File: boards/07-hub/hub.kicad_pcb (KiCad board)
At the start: 2 copper layers, 130 x 98 mm, 28 parts, among them J1 USB_B, J2 BUS, J3 BUS, J4 BUS, J5 BUS, J6 BUS, J7 BUS, J8 BUS, J9 BUS

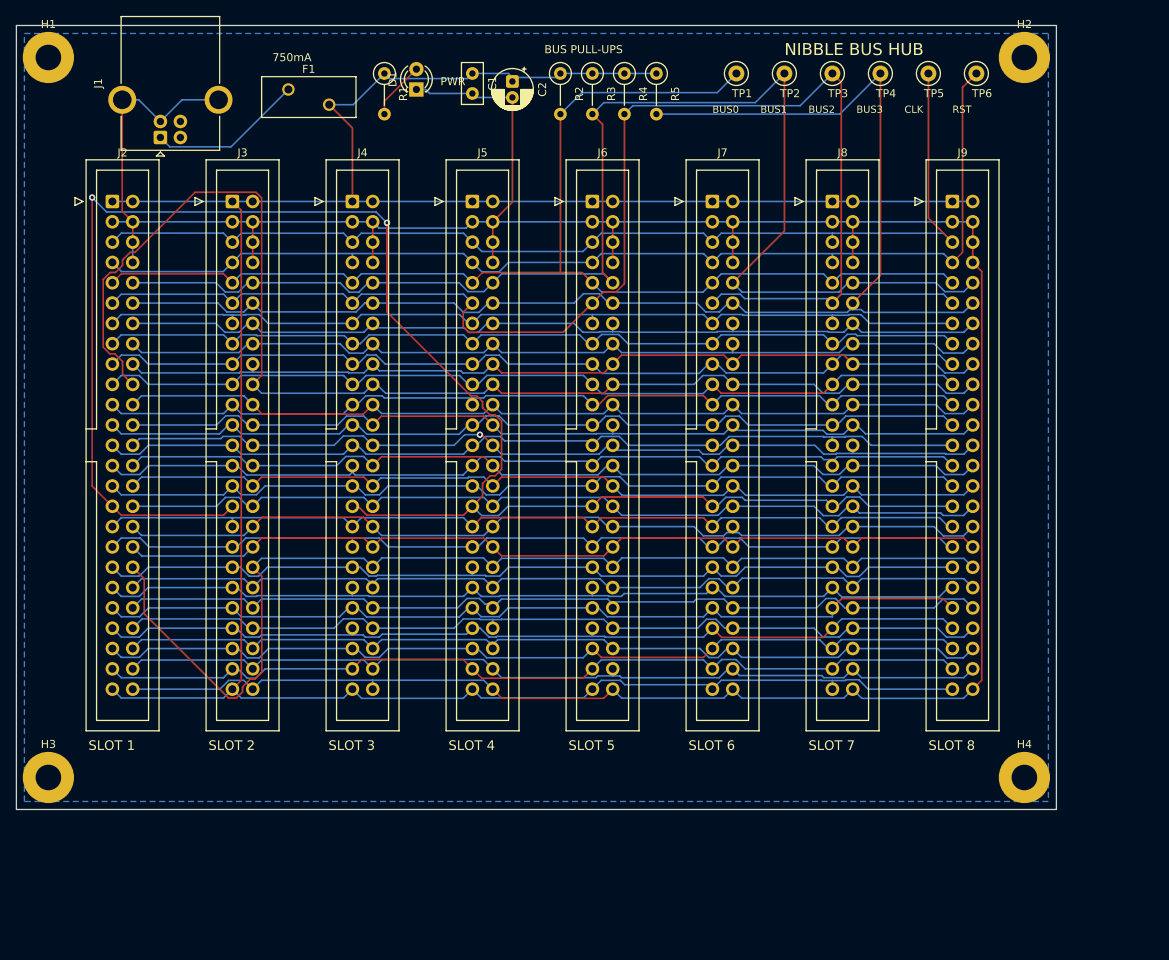
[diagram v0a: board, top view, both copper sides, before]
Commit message: Hub routed: DRC zero, nothing unconnected
The test loops sat on the corner mounting hole and on the last header's
courtyard; they are a 3 x 2 block between the bus pull-ups and the hole now.

Co-Authored-By: Claude Fable 5.1 <noreply@anthropic.com>
Claude-Session: https://claude.ai/code/session_019vcbW37ERmrjZaWq55Er3J
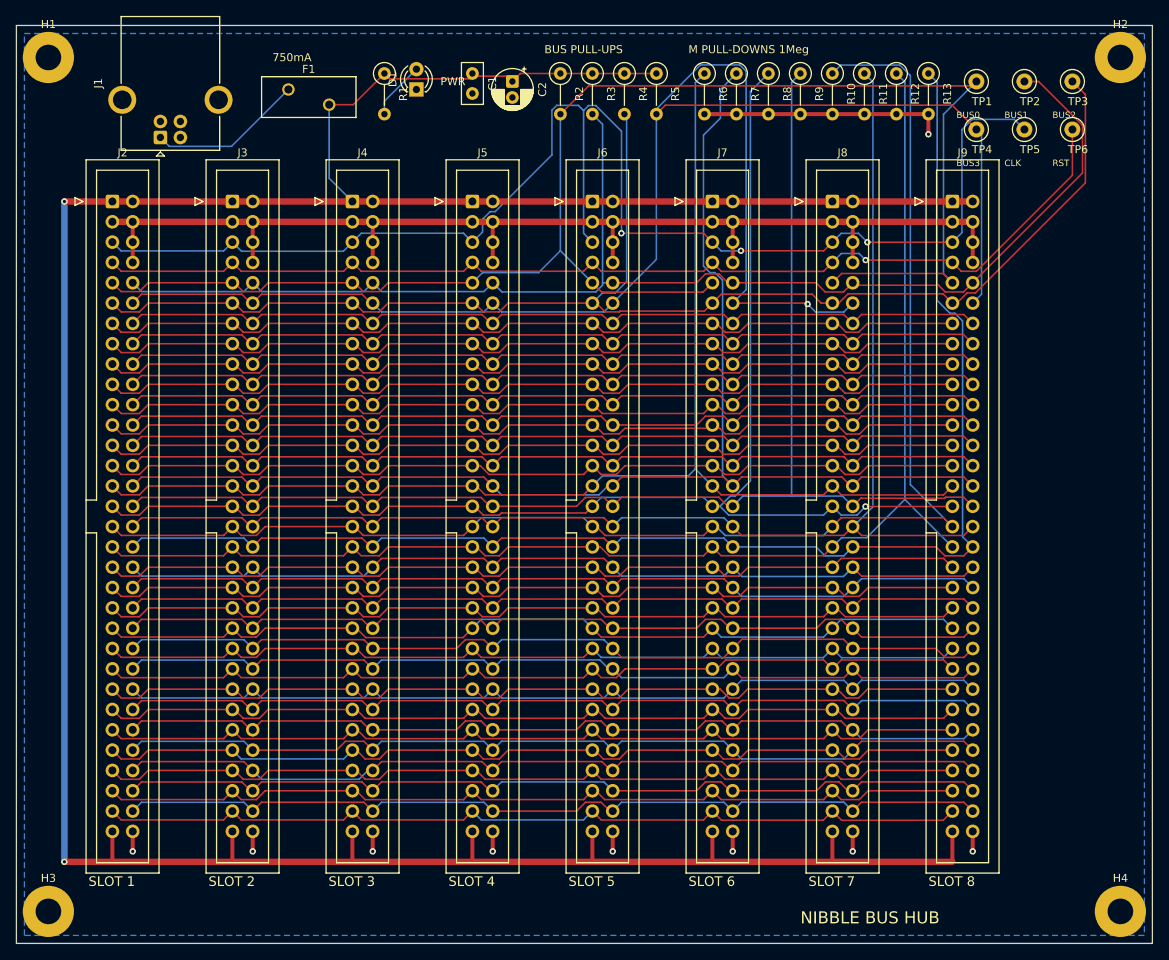
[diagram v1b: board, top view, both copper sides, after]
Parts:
- added R10: 1Meg, R_Axial_DIN0207_L6.3mm_D2.5mm_P5.08mm_Vertical, F.Cu at (102.0, 6.00)
- added R11: 1Meg, R_Axial_DIN0207_L6.3mm_D2.5mm_P5.08mm_Vertical, F.Cu at (106.0, 6.00)
- added R12: 1Meg, R_Axial_DIN0207_L6.3mm_D2.5mm_P5.08mm_Vertical, F.Cu at (110.0, 6.00)
- added R13: 1Meg, R_Axial_DIN0207_L6.3mm_D2.5mm_P5.08mm_Vertical, F.Cu at (114.0, 6.00)
- added R6: 1Meg, R_Axial_DIN0207_L6.3mm_D2.5mm_P5.08mm_Vertical, F.Cu at (86.0, 6.00)
- added R7: 1Meg, R_Axial_DIN0207_L6.3mm_D2.5mm_P5.08mm_Vertical, F.Cu at (90.0, 6.00)
- added R8: 1Meg, R_Axial_DIN0207_L6.3mm_D2.5mm_P5.08mm_Vertical, F.Cu at (94.0, 6.00)
- added R9: 1Meg, R_Axial_DIN0207_L6.3mm_D2.5mm_P5.08mm_Vertical, F.Cu at (98.0, 6.00)
- J2, J3, J4, J5, J6, J7, J8, J9: footprint IDC-Header_2x25_P2.54mm_Vertical -> IDC-Header_2x32_P2.54mm_Vertical
- moved TP1 30.0 mm to (120.0, 7.00)
- moved TP2 30.0 mm to (126.0, 7.00)
- moved TP3 30.0 mm to (132.0, 7.00)
- moved H4 20.6 mm to (138.0, 110.7)
- moved H3 16.7 mm to (4.00, 110.7)
- moved TP4 13.9 mm to (120.0, 13.0)
- moved TP5 13.9 mm to (126.0, 13.0)
- moved TP6 13.9 mm to (132.0, 13.0)
- moved H2 12.0 mm to (138.0, 4.00)
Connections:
- J2 pad 25: M0 -> PC4
- J2 pad 26: M1 -> PC5
- J2 pad 27: M2 -> PC6
- J2 pad 28: M3 -> PC7
- J2 pad 29: M4 -> M0
- J2 pad 30: M5 -> M1
- J2 pad 31: M6 -> M2
- J2 pad 32: M7 -> M3
- J2 pad 33: CF -> M4
- J2 pad 34: ZF -> M5
- J2 pad 35: SUB -> M6
- J2 pad 36: EO -> M7
- J2 pad 37: AI -> CF
- J2 pad 38: AO -> ZF
- J2 pad 39: BI -> SUB
- J2 pad 40: BA -> EO
- J2 pad 41: AB -> AI
- J2 pad 42: OI -> AO
- J2 pad 43: IO -> BI
- J2 pad 44: II -> BO
- J2 pad 45: PCE -> BA
- J2 pad 46: PCL -> AB
- J2 pad 47: FI -> OI
- J2 pad 48: HLT -> IO
- J2 pad 49: +5V -> II
- J2 pad 50: GND -> PCE
- J3 pad 25: M0 -> PC4
- J3 pad 26: M1 -> PC5
- J3 pad 27: M2 -> PC6
- J3 pad 28: M3 -> PC7
- J3 pad 29: M4 -> M0
- J3 pad 30: M5 -> M1
- J3 pad 31: M6 -> M2
- J3 pad 32: M7 -> M3
- J3 pad 33: CF -> M4
- J3 pad 34: ZF -> M5
- J3 pad 35: SUB -> M6
- J3 pad 36: EO -> M7
- J3 pad 37: AI -> CF
- J3 pad 38: AO -> ZF
- J3 pad 39: BI -> SUB
- J3 pad 40: BA -> EO
- J3 pad 41: AB -> AI
- J3 pad 42: OI -> AO
- J3 pad 43: IO -> BI
- J3 pad 44: II -> BO
- J3 pad 45: PCE -> BA
- J3 pad 46: PCL -> AB
- J3 pad 47: FI -> OI
- J3 pad 48: HLT -> IO
- J3 pad 49: +5V -> II
- J3 pad 50: GND -> PCE
- J4 pad 25: M0 -> PC4
- J4 pad 26: M1 -> PC5
- J4 pad 27: M2 -> PC6
- J4 pad 28: M3 -> PC7
- J4 pad 29: M4 -> M0
- J4 pad 30: M5 -> M1
- J4 pad 31: M6 -> M2
- J4 pad 32: M7 -> M3
- J4 pad 33: CF -> M4
- J4 pad 34: ZF -> M5
- J4 pad 35: SUB -> M6
- J4 pad 36: EO -> M7
- J4 pad 37: AI -> CF
- J4 pad 38: AO -> ZF
- J4 pad 39: BI -> SUB
- J4 pad 40: BA -> EO
- J4 pad 41: AB -> AI
- J4 pad 42: OI -> AO
- J4 pad 43: IO -> BI
- J4 pad 44: II -> BO
- J4 pad 45: PCE -> BA
- J4 pad 46: PCL -> AB
- J4 pad 47: FI -> OI
- J4 pad 48: HLT -> IO
- J4 pad 49: +5V -> II
- J4 pad 50: GND -> PCE
- J5 pad 25: M0 -> PC4
- J5 pad 26: M1 -> PC5
- J5 pad 27: M2 -> PC6
- J5 pad 28: M3 -> PC7
- J5 pad 29: M4 -> M0
- J5 pad 30: M5 -> M1
- J5 pad 31: M6 -> M2
- J5 pad 32: M7 -> M3
- J5 pad 33: CF -> M4
- J5 pad 34: ZF -> M5
- J5 pad 35: SUB -> M6
- J5 pad 36: EO -> M7
- J5 pad 37: AI -> CF
- J5 pad 38: AO -> ZF
- J5 pad 39: BI -> SUB
- J5 pad 40: BA -> EO
- J5 pad 41: AB -> AI
- J5 pad 42: OI -> AO
- J5 pad 43: IO -> BI
- J5 pad 44: II -> BO
- J5 pad 45: PCE -> BA
- J5 pad 46: PCL -> AB
- J5 pad 47: FI -> OI
- J5 pad 48: HLT -> IO
- J5 pad 49: +5V -> II
- J5 pad 50: GND -> PCE
- J6 pad 25: M0 -> PC4
- J6 pad 26: M1 -> PC5
- J6 pad 27: M2 -> PC6
- J6 pad 28: M3 -> PC7
- J6 pad 29: M4 -> M0
- J6 pad 30: M5 -> M1
- J6 pad 31: M6 -> M2
- J6 pad 32: M7 -> M3
- J6 pad 33: CF -> M4
- J6 pad 34: ZF -> M5
- J6 pad 35: SUB -> M6
- J6 pad 36: EO -> M7
- J6 pad 37: AI -> CF
- J6 pad 38: AO -> ZF
- J6 pad 39: BI -> SUB
- J6 pad 40: BA -> EO
- J6 pad 41: AB -> AI
- J6 pad 42: OI -> AO
- J6 pad 43: IO -> BI
- J6 pad 44: II -> BO
- J6 pad 45: PCE -> BA
- J6 pad 46: PCL -> AB
- J6 pad 47: FI -> OI
- J6 pad 48: HLT -> IO
- J6 pad 49: +5V -> II
- J6 pad 50: GND -> PCE
- J7 pad 25: M0 -> PC4
- J7 pad 26: M1 -> PC5
- J7 pad 27: M2 -> PC6
- J7 pad 28: M3 -> PC7
- J7 pad 29: M4 -> M0
- J7 pad 30: M5 -> M1
- J7 pad 31: M6 -> M2
- J7 pad 32: M7 -> M3
- J7 pad 33: CF -> M4
- J7 pad 34: ZF -> M5
- J7 pad 35: SUB -> M6
- J7 pad 36: EO -> M7
- J7 pad 37: AI -> CF
- J7 pad 38: AO -> ZF
- J7 pad 39: BI -> SUB
- J7 pad 40: BA -> EO
- J7 pad 41: AB -> AI
- J7 pad 42: OI -> AO
- J7 pad 43: IO -> BI
- J7 pad 44: II -> BO
- J7 pad 45: PCE -> BA
- J7 pad 46: PCL -> AB
- J7 pad 47: FI -> OI
- J7 pad 48: HLT -> IO
- J7 pad 49: +5V -> II
- J7 pad 50: GND -> PCE
- J8 pad 25: M0 -> PC4
- J8 pad 26: M1 -> PC5
- J8 pad 27: M2 -> PC6
- J8 pad 28: M3 -> PC7
- J8 pad 29: M4 -> M0
- J8 pad 30: M5 -> M1
- J8 pad 31: M6 -> M2
- J8 pad 32: M7 -> M3
- J8 pad 33: CF -> M4
- J8 pad 34: ZF -> M5
- J8 pad 35: SUB -> M6
- J8 pad 36: EO -> M7
- J8 pad 37: AI -> CF
- J8 pad 38: AO -> ZF
- J8 pad 39: BI -> SUB
- J8 pad 40: BA -> EO
- J8 pad 41: AB -> AI
- J8 pad 42: OI -> AO
- J8 pad 43: IO -> BI
- J8 pad 44: II -> BO
- J8 pad 45: PCE -> BA
- J8 pad 46: PCL -> AB
- J8 pad 47: FI -> OI
- J8 pad 48: HLT -> IO
- J8 pad 49: +5V -> II
- J8 pad 50: GND -> PCE
- J9 pad 25: M0 -> PC4
- J9 pad 26: M1 -> PC5
- J9 pad 27: M2 -> PC6
- J9 pad 28: M3 -> PC7
- J9 pad 29: M4 -> M0
- J9 pad 30: M5 -> M1
- J9 pad 31: M6 -> M2
- J9 pad 32: M7 -> M3
- J9 pad 33: CF -> M4
- J9 pad 34: ZF -> M5
- J9 pad 35: SUB -> M6
- J9 pad 36: EO -> M7
- J9 pad 37: AI -> CF
- J9 pad 38: AO -> ZF
- J9 pad 39: BI -> SUB
- J9 pad 40: BA -> EO
- J9 pad 41: AB -> AI
- J9 pad 42: OI -> AO
- J9 pad 43: IO -> BI
- J9 pad 44: II -> BO
- J9 pad 45: PCE -> BA
- J9 pad 46: PCL -> AB
- J9 pad 47: FI -> OI
- J9 pad 48: HLT -> IO
- J9 pad 49: +5V -> II
- J9 pad 50: GND -> PCE
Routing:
- net GND: track 373.9 -> 198.7 mm, vias 0 -> 9
- net PC5: track 0.00 -> 111.5 mm
- net F1: track 0.00 -> 111.5 mm
- net PC7: track 0.00 -> 111.4 mm
- net BO: track 0.00 -> 111.4 mm
- net MO: track 0.00 -> 111.4 mm
- net MAI: track 0.00 -> 111.4 mm
- net ONE: track 0.00 -> 111.4 mm
- net PC4: track 0.00 -> 111.4 mm
- net WRL: track 0.00 -> 111.4 mm
- net WRH: track 0.00 -> 111.4 mm
- net MI: track 0.00 -> 111.4 mm
- net F0: track 0.00 -> 111.4 mm
- net PC6: track 0.00 -> 111.4 mm
- net INP: track 0.00 -> 111.4 mm
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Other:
- board size 130 x 98 mm -> 142 x 114.7 mm
- board text added: "M PULL-DOWNS 1Meg"
